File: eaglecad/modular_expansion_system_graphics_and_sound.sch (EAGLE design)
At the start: 63 parts, among them IC1_JOY2_BUF 74LS244N, IC2_GLU ATF22V10, IC3 74LS74N, IC8_JOY1_BUF 74LS244N, IC9-74HCU04 74LS04N, J1-INTERRUPTS INTERRUPTS, J1_ADDRESS_CON j1, J2-WAITS WAITS, J2_DATA_AND_POWER_CON j2, J3-VIDEO-OUT RCA, J4-AUDIO-LEFT RCA, J5-AUDIO-RIGHT RCA, Q2 2N2222, U11_SND1 SN76489, U1_TMS_RAM TMS4416, U2_VDP TMS9118, U3_TMS_RAM TMS4416, U4_SND2 SN76489, U5_SND3 SN76489, U6_SND4 SN76489, Y1 OSC1-CPP-4

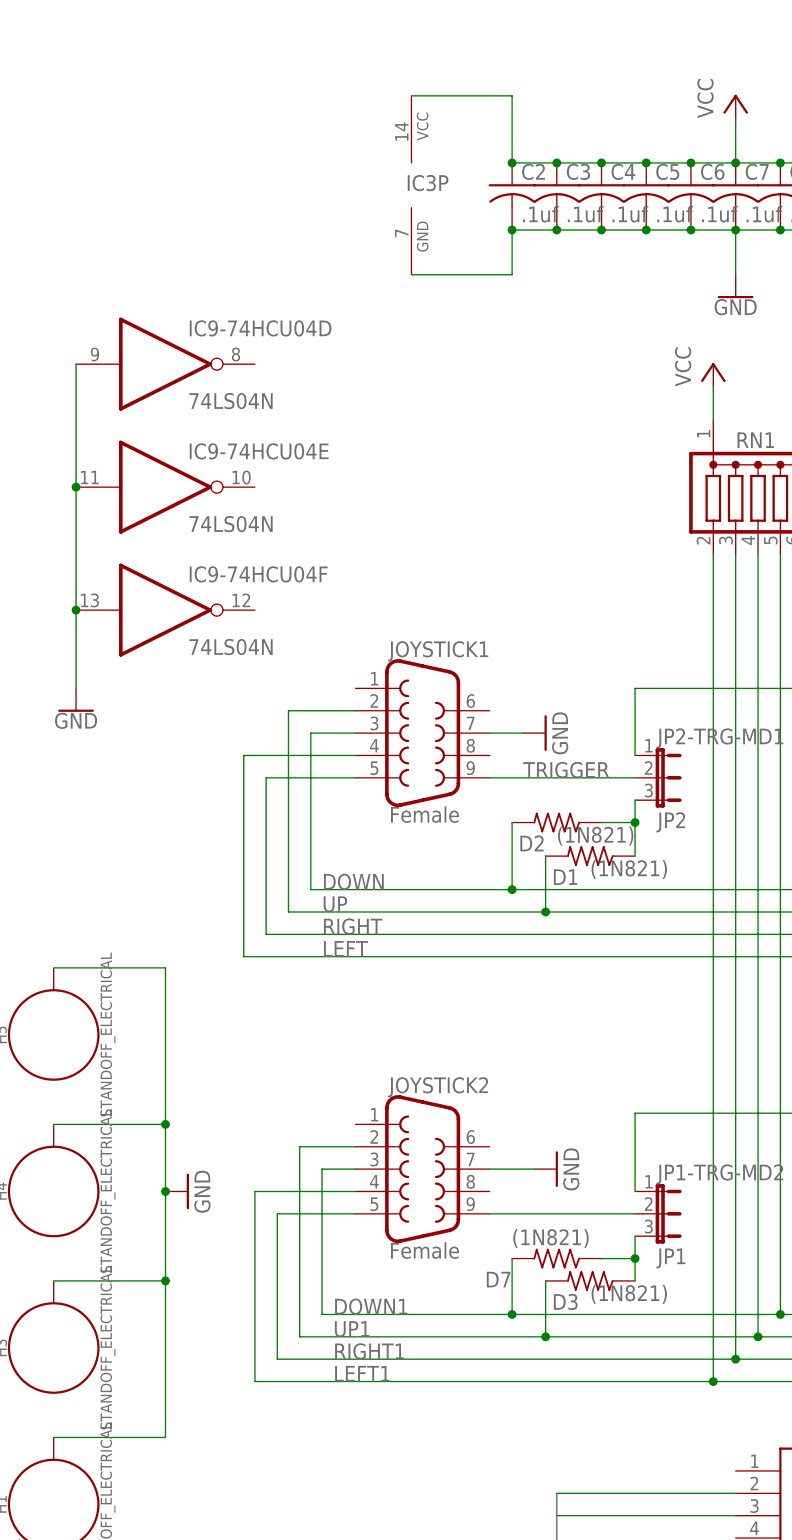
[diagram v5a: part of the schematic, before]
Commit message: updated graphics board to make joysticks compatible with old games
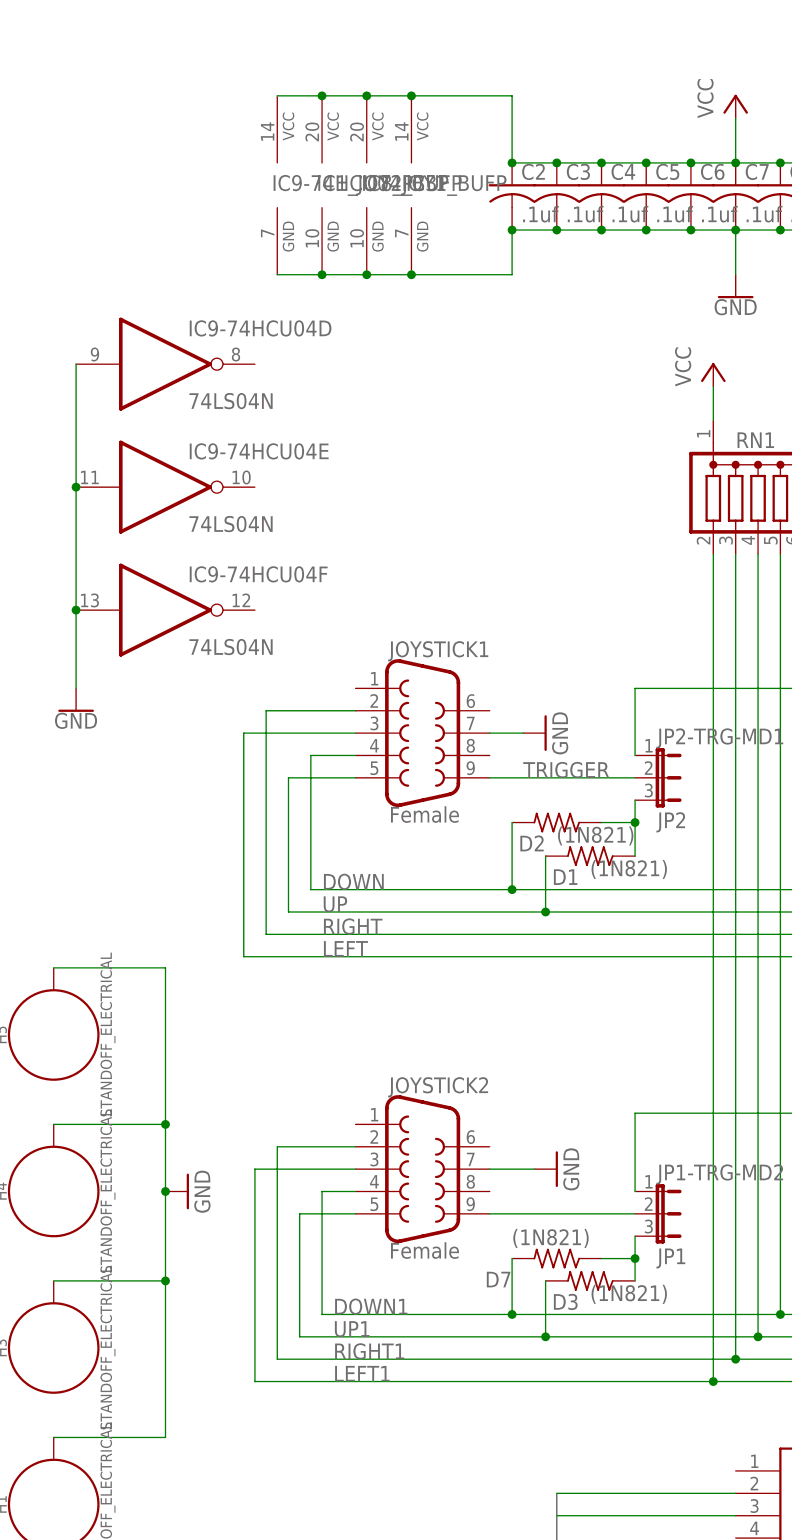
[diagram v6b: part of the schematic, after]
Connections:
- net JOY1_IN_ENABLE_N1 renamed JOY2_IN_ENABLE_N
- net N$11 renamed TIED-HIGH-1
- net N$20 renamed TIED-HIGH-2
- net DOWN: now also JOYSTICK1.4; no longer JOYSTICK1.3
- net DOWN1: now also JOYSTICK2.4; no longer JOYSTICK2.3
- net GND: now also IC1_JOY2_BUFP.GND, IC8_JOY1_BUFP.GND, IC9-74HCU04P.GND
- net LEFT: now also JOYSTICK1.3; no longer JOYSTICK1.4
- net LEFT1: now also JOYSTICK2.3; no longer JOYSTICK2.4
- net RIGHT: now also JOYSTICK1.2; no longer JOYSTICK1.5
- net RIGHT1: now also JOYSTICK2.2; no longer JOYSTICK2.5
- net UP: now also JOYSTICK1.5; no longer JOYSTICK1.2
- net UP1: now also JOYSTICK2.5; no longer JOYSTICK2.2
- net VCC: now also IC1_JOY2_BUFP.VCC, IC8_JOY1_BUFP.VCC, IC9-74HCU04P.VCC
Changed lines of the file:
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@@
 <attribute name="VALUE" x="114.3" y="226.822" size="1.778" layer="96" rot="R180"/>
+</instance>
+<instance part="IC8_JOY1_BUF" gate="P" x="83.82" y="299.72" smashed="yes">
+<attribute name="NAME" x="83.185" y="299.085" size="1.778" layer="95"/>
+</instance>
+<instance part="IC1_JOY2_BUF" gate="P" x="78.74" y="299.72" smashed="yes">
+<attribute name="NAME" x="78.105" y="299.085" size="1.778" layer="95"/>
+</instance>
+<instance part="IC9-74HCU04" gate="P" x="73.66" y="299.72" smashed="yes">
+<attribute name="NAME" x="73.025" y="299.085" size="1.778" layer="95"/>
 </instance>
 </instances>
@@
 <wire x1="100.33" y1="289.56" x2="100.33" y2="294.64" width="0.1524" layer="91"/>
 <junction x="100.33" y="294.64"/>
+<pinref part="IC8_JOY1_BUF" gate="P" pin="GND"/>
+<wire x1="88.9" y1="289.56" x2="83.82" y2="289.56" width="0.1524" layer="91"/>
+<junction x="88.9" y="289.56"/>
+<pinref part="IC1_JOY2_BUF" gate="P" pin="GND"/>
+<wire x1="83.82" y1="289.56" x2="78.74" y2="289.56" width="0.1524" layer="91"/>
+<junction x="83.82" y="289.56"/>
+<pinref part="IC9-74HCU04" gate="P" pin="GND"/>
+<wire x1="78.74" y1="289.56" x2="73.66" y2="289.56" width="0.1524" layer="91"/>
+<junction x="78.74" y="289.56"/>
 </segment>
 <segment>
@@
 <wire x1="100.33" y1="309.88" x2="100.33" y2="302.26" width="0.1524" layer="91"/>
 <junction x="100.33" y="302.26"/>
+<pinref part="IC8_JOY1_BUF" gate="P" pin="VCC"/>
+<wire x1="88.9" y1="309.88" x2="83.82" y2="309.88" width="0.1524" layer="91"/>
+<junction x="88.9" y="309.88"/>
+<pinref part="IC1_JOY2_BUF" gate="P" pin="VCC"/>
+<wire x1="83.82" y1="309.88" x2="78.74" y2="309.88" width="0.1524" layer="91"/>
+<junction x="83.82" y="309.88"/>
+<pinref part="IC9-74HCU04" gate="P" pin="VCC"/>
+<wire x1="78.74" y1="309.88" x2="73.66" y2="309.88" width="0.1524" layer="91"/>
+<junction x="78.74" y="309.88"/>
 </segment>
 <segment>
@@
 <net name="UP" class="0">
 <segment>
-<pinref part="JOYSTICK1" gate="G$1" pin="2"/>
-<wire x1="82.55" y1="240.03" x2="74.93" y2="240.03" width="0.1524" layer="91"/>
-<wire x1="74.93" y1="240.03" x2="74.93" y2="217.17" width="0.1524" layer="91"/>
 <pinref part="IC8_JOY1_BUF" gate="B" pin="A4"/>
 <wire x1="74.93" y1="217.17" x2="104.14" y2="217.17" width="0.1524" layer="91"/>
@@
 <junction x="143.51" y="217.17"/>
 <pinref part="D1" gate="G$1" pin="2"/>
+<pinref part="JOYSTICK1" gate="G$1" pin="5"/>
+<wire x1="82.55" y1="232.41" x2="74.93" y2="232.41" width="0.1524" layer="91"/>
+<wire x1="74.93" y1="217.17" x2="74.93" y2="232.41" width="0.1524" layer="91"/>
 </segment>
 </net>
 <net name="DOWN" class="0">
 <segment>
-<pinref part="JOYSTICK1" gate="G$1" pin="3"/>
-<wire x1="82.55" y1="237.49" x2="77.47" y2="237.49" width="0.1524" layer="91"/>
 <pinref part="IC8_JOY1_BUF" gate="B" pin="A3"/>
 <wire x1="161.29" y1="219.71" x2="146.05" y2="219.71" width="0.1524" layer="91"/>
 <wire x1="146.05" y1="219.71" x2="100.33" y2="219.71" width="0.1524" layer="91"/>
 <wire x1="100.33" y1="219.71" x2="77.47" y2="219.71" width="0.1524" layer="91"/>
-<wire x1="77.47" y1="219.71" x2="77.47" y2="237.49" width="0.1524" layer="91"/>
 <label x="78.74" y="219.71" size="1.778" layer="95"/>
 <wire x1="100.33" y1="227.33" x2="100.33" y2="219.71" width="0.1524" layer="91"/>
@@
 <junction x="146.05" y="219.71"/>
 <pinref part="D2" gate="G$1" pin="2"/>
+<pinref part="JOYSTICK1" gate="G$1" pin="4"/>
+<wire x1="82.55" y1="234.95" x2="77.47" y2="234.95" width="0.1524" layer="91"/>
+<wire x1="77.47" y1="234.95" x2="77.47" y2="219.71" width="0.1524" layer="91"/>
 </segment>
 </net>
 <net name="LEFT" class="0">
 <segment>
-<pinref part="JOYSTICK1" gate="G$1" pin="4"/>
-<wire x1="82.55" y1="234.95" x2="69.85" y2="234.95" width="0.1524" layer="91"/>
 <pinref part="IC8_JOY1_BUF" gate="B" pin="A2"/>
 <wire x1="161.29" y1="222.25" x2="153.67" y2="222.25" width="0.1524" layer="91"/>
@@
 <wire x1="153.67" y1="212.09" x2="138.43" y2="212.09" width="0.1524" layer="91"/>
 <wire x1="138.43" y1="212.09" x2="69.85" y2="212.09" width="0.1524" layer="91"/>
-<wire x1="69.85" y1="212.09" x2="69.85" y2="234.95" width="0.1524" layer="91"/>
+<wire x1="69.85" y1="212.09" x2="69.85" y2="237.49" width="0.1524" layer="91"/>
 <label x="78.74" y="212.09" size="1.778" layer="95"/>
 <pinref part="RN1" gate="A" pin="8"/>
 <wire x1="138.43" y1="257.81" x2="138.43" y2="212.09" width="0.1524" layer="91"/>
 <junction x="138.43" y="212.09"/>
+<pinref part="JOYSTICK1" gate="G$1" pin="3"/>
+<wire x1="82.55" y1="237.49" x2="69.85" y2="237.49" width="0.1524" layer="91"/>
 </segment>
 </net>
 <net name="RIGHT" class="0">
 <segment>
-<pinref part="JOYSTICK1" gate="G$1" pin="5"/>
-<wire x1="82.55" y1="232.41" x2="72.39" y2="232.41" width="0.1524" layer="91"/>
 <label x="78.74" y="214.63" size="1.778" layer="95"/>
 <pinref part="IC8_JOY1_BUF" gate="B" pin="A1"/>
@@
 <wire x1="151.13" y1="214.63" x2="140.97" y2="214.63" width="0.1524" layer="91"/>
 <wire x1="140.97" y1="214.63" x2="72.39" y2="214.63" width="0.1524" layer="91"/>
-<wire x1="72.39" y1="214.63" x2="72.39" y2="232.41" width="0.1524" layer="91"/>
 <pinref part="RN1" gate="A" pin="9"/>
 <wire x1="140.97" y1="257.81" x2="140.97" y2="214.63" width="0.1524" layer="91"/>
 <junction x="140.97" y="214.63"/>
+<pinref part="JOYSTICK1" gate="G$1" pin="2"/>
+<wire x1="82.55" y1="240.03" x2="72.39" y2="240.03" width="0.1524" layer="91"/>
+<wire x1="72.39" y1="240.03" x2="72.39" y2="214.63" width="0.1524" layer="91"/>
 </segment>
 </net>
@@
 <net name="UP1" class="0">
 <segment>
-<pinref part="JOYSTICK2" gate="G$1" pin="2"/>
-<wire x1="82.55" y1="190.5" x2="76.2" y2="190.5" width="0.1524" layer="91"/>
 <label x="80.01" y="168.91" size="1.778" layer="95"/>
 <pinref part="IC1_JOY2_BUF" gate="B" pin="A4"/>
@@
 <wire x1="128.27" y1="168.91" x2="104.14" y2="168.91" width="0.1524" layer="91"/>
 <wire x1="104.14" y1="168.91" x2="76.2" y2="168.91" width="0.1524" layer="91"/>
-<wire x1="76.2" y1="168.91" x2="76.2" y2="190.5" width="0.1524" layer="91"/>
 <wire x1="104.14" y1="175.26" x2="104.14" y2="168.91" width="0.1524" layer="91"/>
 <junction x="104.14" y="168.91"/>
@@
 <junction x="128.27" y="168.91"/>
 <pinref part="D3" gate="G$1" pin="2"/>
+<pinref part="JOYSTICK2" gate="G$1" pin="5"/>
+<wire x1="82.55" y1="182.88" x2="76.2" y2="182.88" width="0.1524" layer="91"/>
+<wire x1="76.2" y1="182.88" x2="76.2" y2="168.91" width="0.1524" layer="91"/>
 </segment>
 </net>
 <net name="DOWN1" class="0">
 <segment>
-<pinref part="JOYSTICK2" gate="G$1" pin="3"/>
-<wire x1="82.55" y1="187.96" x2="78.74" y2="187.96" width="0.1524" layer="91"/>
 <label x="80.01" y="171.45" size="1.778" layer="95"/>
 <pinref part="IC1_JOY2_BUF" gate="B" pin="A3"/>
@@
 <wire x1="130.81" y1="171.45" x2="100.33" y2="171.45" width="0.1524" layer="91"/>
 <wire x1="100.33" y1="171.45" x2="78.74" y2="171.45" width="0.1524" layer="91"/>
-<wire x1="78.74" y1="171.45" x2="78.74" y2="187.96" width="0.1524" layer="91"/>
 <junction x="100.33" y="171.45"/>
 <pinref part="RN1" gate="A" pin="5"/>
@@
 <pinref part="D7" gate="G$1" pin="2"/>
 <wire x1="100.33" y1="177.8" x2="100.33" y2="171.45" width="0.1524" layer="91"/>
+<pinref part="JOYSTICK2" gate="G$1" pin="4"/>
+<wire x1="82.55" y1="185.42" x2="78.74" y2="185.42" width="0.1524" layer="91"/>
+<wire x1="78.74" y1="185.42" x2="78.74" y2="171.45" width="0.1524" layer="91"/>
 </segment>
 </net>
 <net name="LEFT1" class="0">
 <segment>
-<pinref part="JOYSTICK2" gate="G$1" pin="4"/>
-<wire x1="82.55" y1="185.42" x2="71.12" y2="185.42" width="0.1524" layer="91"/>
 <label x="80.01" y="163.83" size="1.778" layer="95"/>
 <pinref part="IC1_JOY2_BUF" gate="B" pin="A2"/>
@@
 <wire x1="153.67" y1="163.83" x2="123.19" y2="163.83" width="0.1524" layer="91"/>
 <wire x1="123.19" y1="163.83" x2="71.12" y2="163.83" width="0.1524" layer="91"/>
-<wire x1="71.12" y1="163.83" x2="71.12" y2="185.42" width="0.1524" layer="91"/>
 <pinref part="RN1" gate="A" pin="2"/>
 <wire x1="123.19" y1="257.81" x2="123.19" y2="163.83" width="0.1524" layer="91"/>
 <junction x="123.19" y="163.83"/>
+<pinref part="JOYSTICK2" gate="G$1" pin="3"/>
+<wire x1="82.55" y1="187.96" x2="71.12" y2="187.96" width="0.1524" layer="91"/>
+<wire x1="71.12" y1="187.96" x2="71.12" y2="163.83" width="0.1524" layer="91"/>
 </segment>
 </net>
 <net name="RIGHT1" class="0">
 <segment>
-<pinref part="JOYSTICK2" gate="G$1" pin="5"/>
-<wire x1="82.55" y1="182.88" x2="73.66" y2="182.88" width="0.1524" layer="91"/>
 <label x="80.01" y="166.37" size="1.778" layer="95"/>
 <pinref part="IC1_JOY2_BUF" gate="B" pin="A1"/>
@@
 <wire x1="151.13" y1="166.37" x2="125.73" y2="166.37" width="0.1524" layer="91"/>
 <wire x1="125.73" y1="166.37" x2="73.66" y2="166.37" width="0.1524" layer="91"/>
-<wire x1="73.66" y1="166.37" x2="73.66" y2="182.88" width="0.1524" layer="91"/>
 <pinref part="RN1" gate="A" pin="3"/>
 <wire x1="125.73" y1="257.81" x2="125.73" y2="166.37" width="0.1524" layer="91"/>
 <junction x="125.73" y="166.37"/>
+<pinref part="JOYSTICK2" gate="G$1" pin="2"/>
+<wire x1="82.55" y1="190.5" x2="73.66" y2="190.5" width="0.1524" layer="91"/>
+<wire x1="73.66" y1="190.5" x2="73.66" y2="166.37" width="0.1524" layer="91"/>
 </segment>
 </net>
@@
 </segment>
 </net>
-<net name="JOY1_IN_ENABLE_N1" class="0">
+<net name="JOY2_IN_ENABLE_N" class="0">
 <segment>
 <pinref part="IC1_JOY2_BUF" gate="B" pin="G"/>
@@
 </segment>
 </net>
-<net name="N$11" class="0">
+<net name="TIED-HIGH-1" class="0">
 <segment>
 <pinref part="IC8_JOY1_BUF" gate="A" pin="A1"/>
@@
 </segment>
 </net>
-<net name="N$20" class="0">
+<net name="TIED-HIGH-2" class="0">
 <segment>
 <pinref part="IC1_JOY2_BUF" gate="A" pin="A1"/>
